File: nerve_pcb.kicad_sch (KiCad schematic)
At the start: 46 parts, among them J1 TC2050-IDC, J2 2171750001, J4 472192001, J5 2x8, J6 2x15, SW1 SPST, SW2 SPST, U1 ld39150dt33-r, U2 STM32F446RET, Y1 8M, Y2 32k768

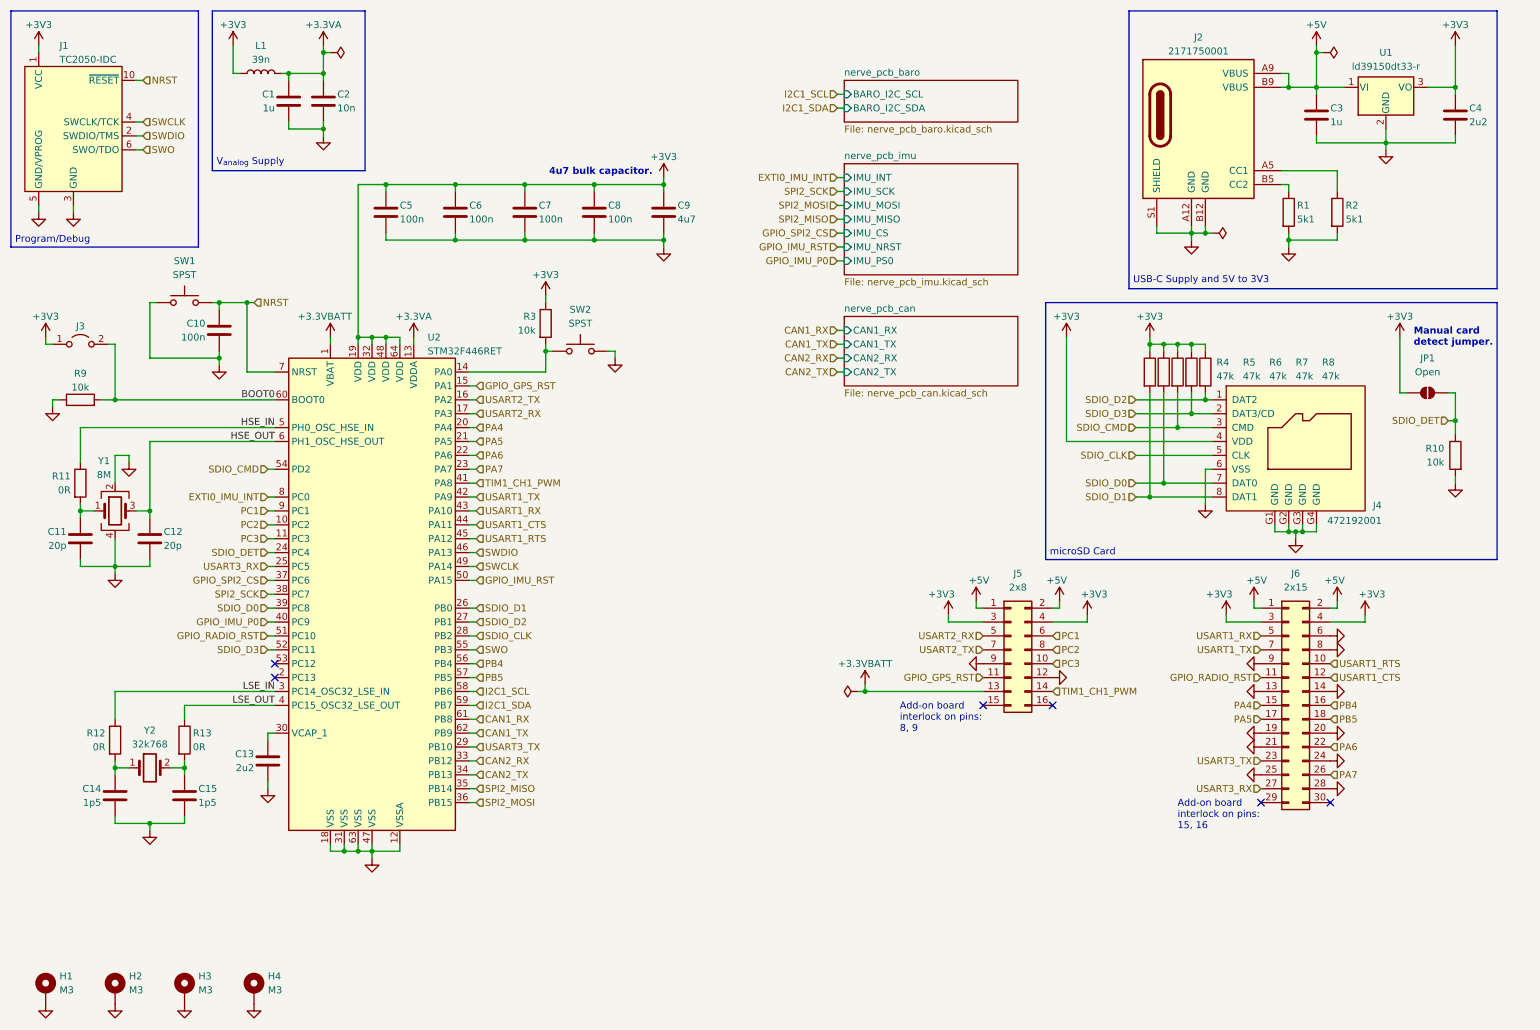
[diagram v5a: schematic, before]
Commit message: Clean up schematics and ensure PCB parity
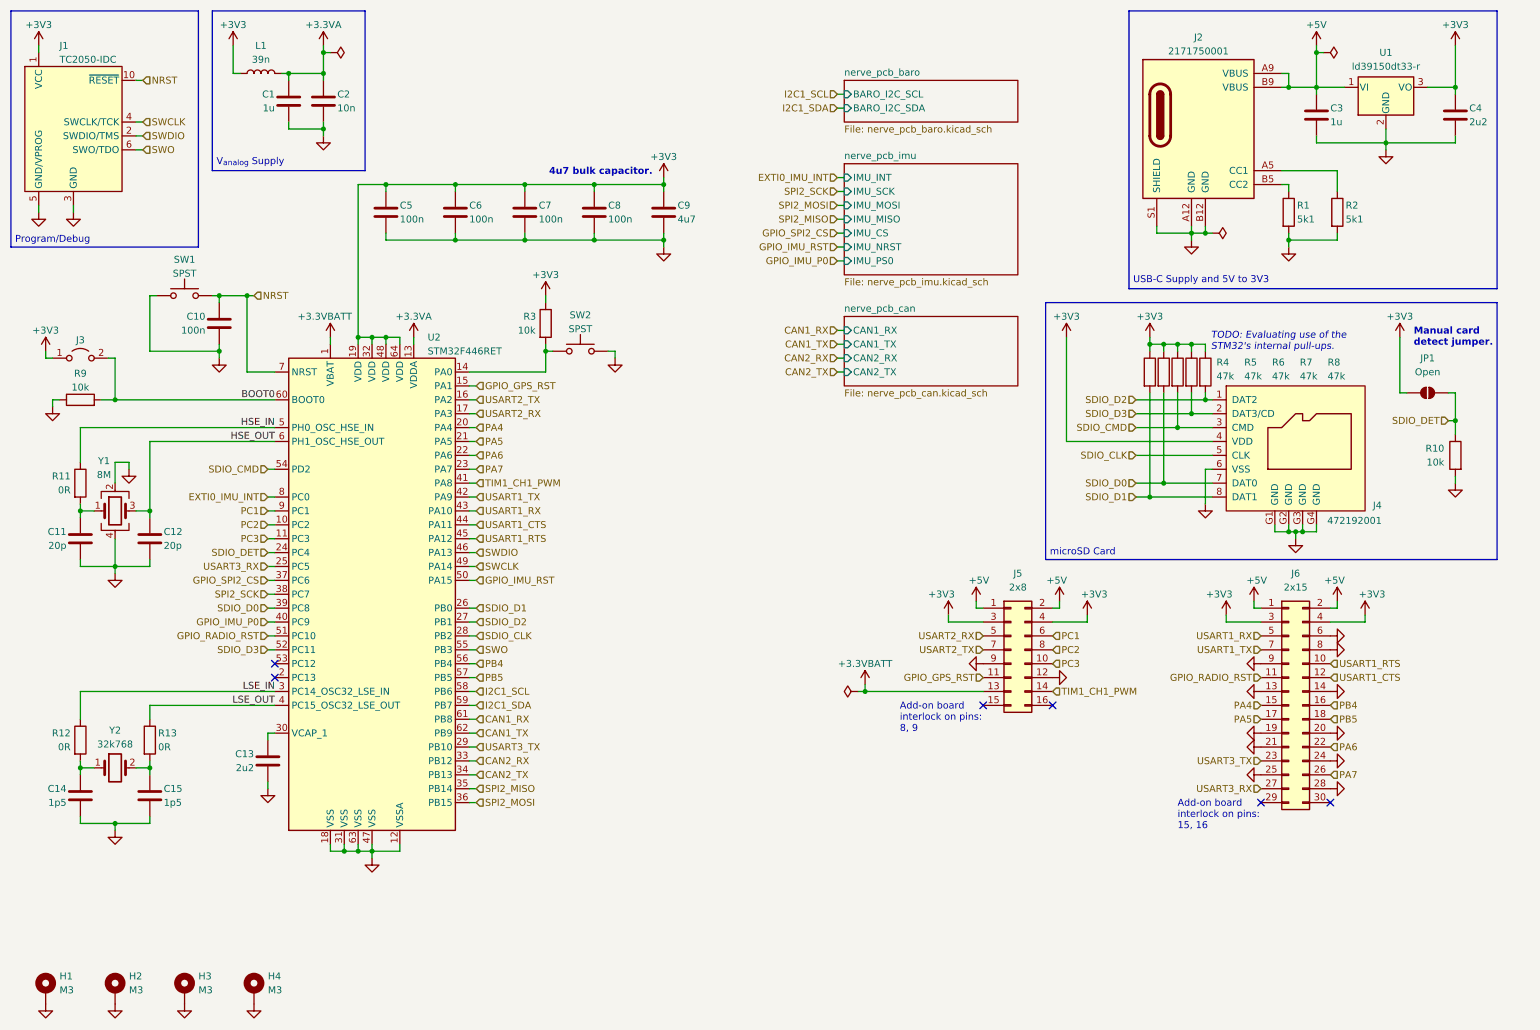
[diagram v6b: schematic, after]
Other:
- note added: "TODO: Evaluating use of the STM32's internal pull-ups."
- moved on the sheet: C10, C14, C15, J3, R12, R13, SW1, Y2

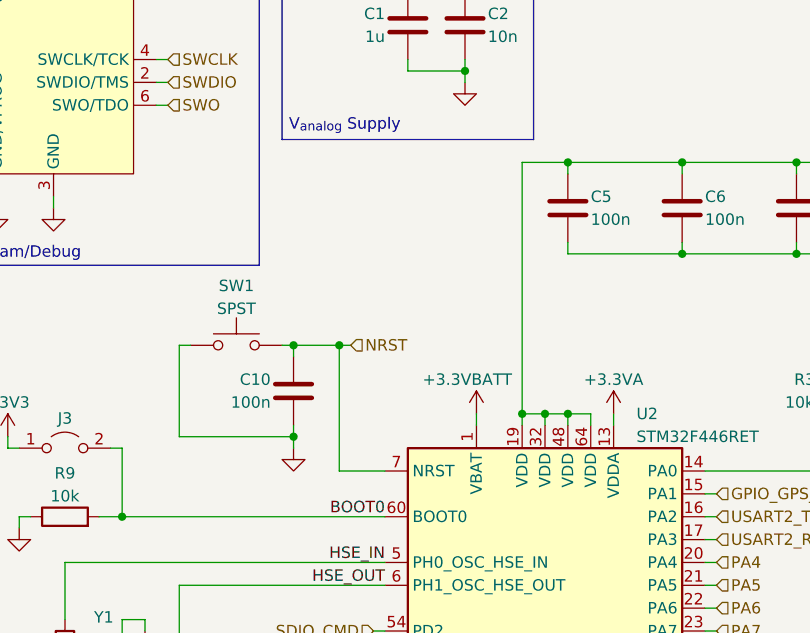
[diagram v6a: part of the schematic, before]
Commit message: Add Vbatt unused jumper
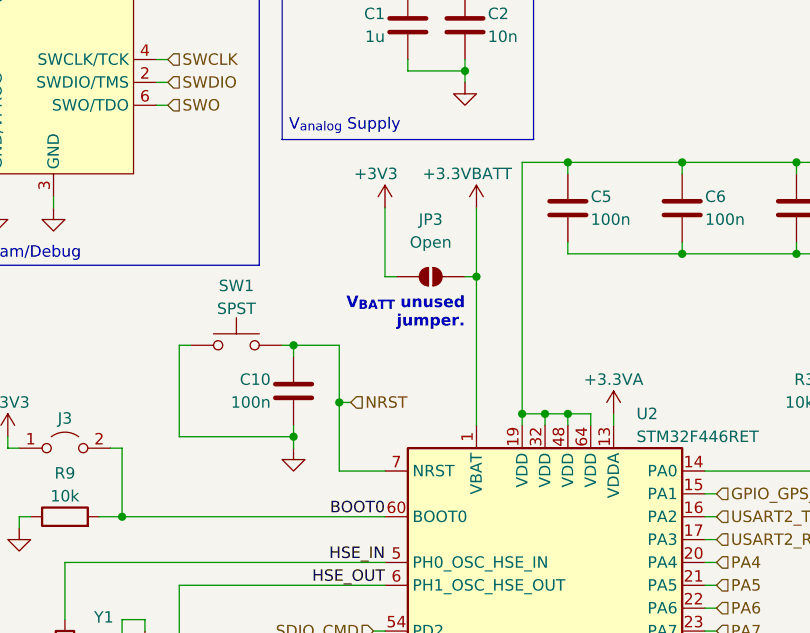
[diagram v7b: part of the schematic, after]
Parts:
- added JP3: Open, Jumper:SolderJumper-2_P1.3mm_Open_TrianglePad1.0x1.5mm, symbol Jumper:SolderJumper_2_Open
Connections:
- net +3.3VBATT: now also JP3.2 (B)
- net +3V3: now also JP3.1 (A)
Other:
- note added: "V_{BATT} unused jumper."
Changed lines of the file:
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@@
 	)
 	(junction
+		(at 71.12 57.15)
+		(diameter 0)
+		(color 0 0 0 0)
+	)
+	(junction
 		(at 246.38 54.61)
 		(diameter 0)
@@
 	)
 	(junction
-		(at 55.88 64.77)
-		(diameter 0)
-		(color 0 0 0 0)
-	)
-	(junction
 		(at 119.38 54.61)
 		(diameter 0)
@@
 	)
 	(junction
+		(at 55.88 71.12)
+		(diameter 0)
+		(color 0 0 0 0)
+	)
+	(junction
 		(at 220.98 101.6)
 		(diameter 0)
@@
 	(wire
 		(pts
+			(xy 71.12 57.15) (xy 71.12 73.66)
+		)
+		(stroke
+			(width 0)
+			(type default)
+		)
+	)
+	(wire
+		(pts
 			(xy 276.86 19.05) (xy 276.86 26.67)
 		)
@@
 	(wire
 		(pts
+			(xy 62.23 57.15) (xy 60.96 57.15)
+		)
+		(stroke
+			(width 0)
+			(type default)
+		)
+	)
+	(wire
+		(pts
 			(xy 38.1 64.77) (xy 38.1 74.93)
 		)
@@
 	(wire
 		(pts
-			(xy 55.88 64.77) (xy 55.88 78.74)
+			(xy 55.88 64.77) (xy 55.88 71.12)
 		)
 		(stroke
@@
 	(wire
 		(pts
+			(xy 60.96 57.15) (xy 60.96 49.53)
+		)
+		(stroke
+			(width 0)
+			(type default)
+		)
+	)
+	(wire
+		(pts
 			(xy 96.52 144.78) (xy 97.79 144.78)
 		)
@@
 	(wire
 		(pts
+			(xy 55.88 71.12) (xy 55.88 78.74)
+		)
+		(stroke
+			(width 0)
+			(type default)
+		)
+	)
+	(wire
+		(pts
 			(xy 31.75 109.22) (xy 31.75 114.3)
 		)
@@
 	(wire
 		(pts
-			(xy 71.12 72.39) (xy 71.12 73.66)
-		)
-		(stroke
-			(width 0)
-			(type default)
-		)
-	)
-	(wire
-		(pts
 			(xy 209.55 124.46) (xy 203.2 124.46)
 		)
@@
 	(wire
 		(pts
+			(xy 71.12 49.53) (xy 71.12 57.15)
+		)
+		(stroke
+			(width 0)
+			(type default)
+		)
+	)
+	(wire
+		(pts
 			(xy 163.83 30.48) (xy 165.1 30.48)
 		)
@@
 	(wire
 		(pts
-			(xy 55.88 64.77) (xy 57.15 64.77)
+			(xy 55.88 71.12) (xy 57.15 71.12)
 		)
 		(stroke
@@
 	(wire
 		(pts
+			(xy 69.85 57.15) (xy 71.12 57.15)
+		)
+		(stroke
+			(width 0)
+			(type default)
+		)
+	)
+	(wire
+		(pts
 			(xy 35.56 25.4) (xy 36.83 25.4)
 		)
@@
 		)
 	)
+	(text "V_{BATT} unused\njumper."
+		(exclude_from_sim no)
+		(at 69.85 61.214 0)
+		(effects
+			(font
+				(size 1.27 1.27)
+				(thickness 0.254)
+				(bold yes)
+			)
+			(justify right)
+		)
+	)
 	(text "USB-C Supply and 5V to 3V3"
 		(exclude_from_sim no)
@@
 	(hierarchical_label "NRST"
 		(shape input)
-		(at 57.15 64.77 0)
+		(at 57.15 71.12 0)
 		(fields_autoplaced yes)
 		(effects
@@
 	(symbol
 		(lib_id "power:+3V3")
-		(at 71.12 72.39 0)
+		(at 71.12 49.53 0)
 		(unit 1)
 		(exclude_from_sim no)
@@
 		(dnp no)
 		(property "Reference" "#PWR015"
-			(at 71.12 76.2 0)
+			(at 71.12 53.34 0)
 			(effects
 				(font
@@
 		)
 		(property "Value" "+3.3VBATT"
-			(at 70.104 68.58 0)
+			(at 70.104 45.72 0)
 			(effects
 				(font
@@
 		)
 		(property "Footprint" ""
-			(at 71.12 72.39 0)
+			(at 71.12 49.53 0)
 			(effects
 				(font
@@
 		)
 		(property "Datasheet" ""
-			(at 71.12 72.39 0)
+			(at 71.12 49.53 0)
 			(effects
 				(font
@@
 		)
 		(property "Description" "Power symbol creates a global label with name \"+3V3\""
-			(at 71.12 72.39 0)
+			(at 71.12 49.53 0)
 			(effects
 				(font
@@
 	)
 	(symbol
+		(lib_id "Jumper:SolderJumper_2_Open")
+		(at 66.04 57.15 0)
+		(unit 1)
+		(exclude_from_sim yes)
+		(in_bom no)
+		(on_board yes)
+		(dnp no)
+		(property "Reference" "JP3"
+			(at 66.04 50.8 0)
+			(effects
+				(font
+					(size 1.27 1.27)
+				)
+			)
+		)
+		(property "Value" "Open"
+			(at 66.04 53.34 0)
+			(effects
+				(font
+					(size 1.27 1.27)
+				)
+			)
+		)
+		(property "Footprint" "Jumper:SolderJumper-2_P1.3mm_Open_TrianglePad1.0x1.5mm"
+			(at 66.04 57.15 0)
+			(effects
+				(font
+					(size 1.27 1.27)
+				)
+				(hide yes)
+			)
+		)
+		(property "Datasheet" "~"
+			(at 66.04 57.15 0)
+			(effects
+				(font
+					(size 1.27 1.27)
+				)
+				(hide yes)
+			)
+		)
+		(property "Description" "Solder Jumper, 2-pole, open"
+			(at 66.04 57.15 0)
+			(effects
+				(font
+					(size 1.27 1.27)
+				)
+				(hide yes)
+			)
+		)
+		(pin "1"
+		)
+		(pin "2"
+		)
+		(instances
+			(project "nerve_pcb"
+				(path "/c0277862-b3f2-4e0e-986f-34702f0543f0"
+					(reference "JP3")
+					(unit 1)
+				)
+			)
+		)
+	)
+	(symbol
 		(lib_id "power:GND")
 		(at 78.74 167.64 0)
@@
 					(unit 1)
 				)
+			)
+		)
+	)
+	(symbol
+		(lib_id "power:+3V3")
+		(at 60.96 49.53 0)
+		(unit 1)
+		(exclude_from_sim no)
+		(in_bom yes)
+		(on_board yes)
+		(dnp no)
+		(property "Reference" "#PWR082"
+			(at 60.96 53.34 0)
+			(effects
+				(font
+					(size 1.27 1.27)
+				)
+				(hide yes)
+			)
+		)
+		(property "Value" "+3V3"
+			(at 59.944 45.72 0)
+			(effects
+				(font
+					(size 1.27 1.27)
+				)
+			)
+		)
+		(property "Footprint" ""
+			(at 60.96 49.53 0)
+			(effects
+				(font
+					(size 1.27 1.27)
+				)
+				(hide yes)
+			)
+		)
+		(property "Datasheet" ""
+			(at 60.96 49.53 0)
+			(effects
+				(font
+					(size 1.27 1.27)
+				)
+				(hide yes)
+			)
+		)
+		(property "Description" "Power symbol creates a global label with name \"+3V3\""
+			(at 60.96 49.53 0)
+			(effects
+				(font
+					(size 1.27 1.27)
+				)
+				(hide yes)
+			)
+		)
+		(pin "1"
+		)
+		(instances
+			(project "nerve_pcb"
+				(path "/c0277862-b3f2-4e0e-986f-34702f0543f0"
+					(reference "#PWR082")
+					(unit 1)
+				)

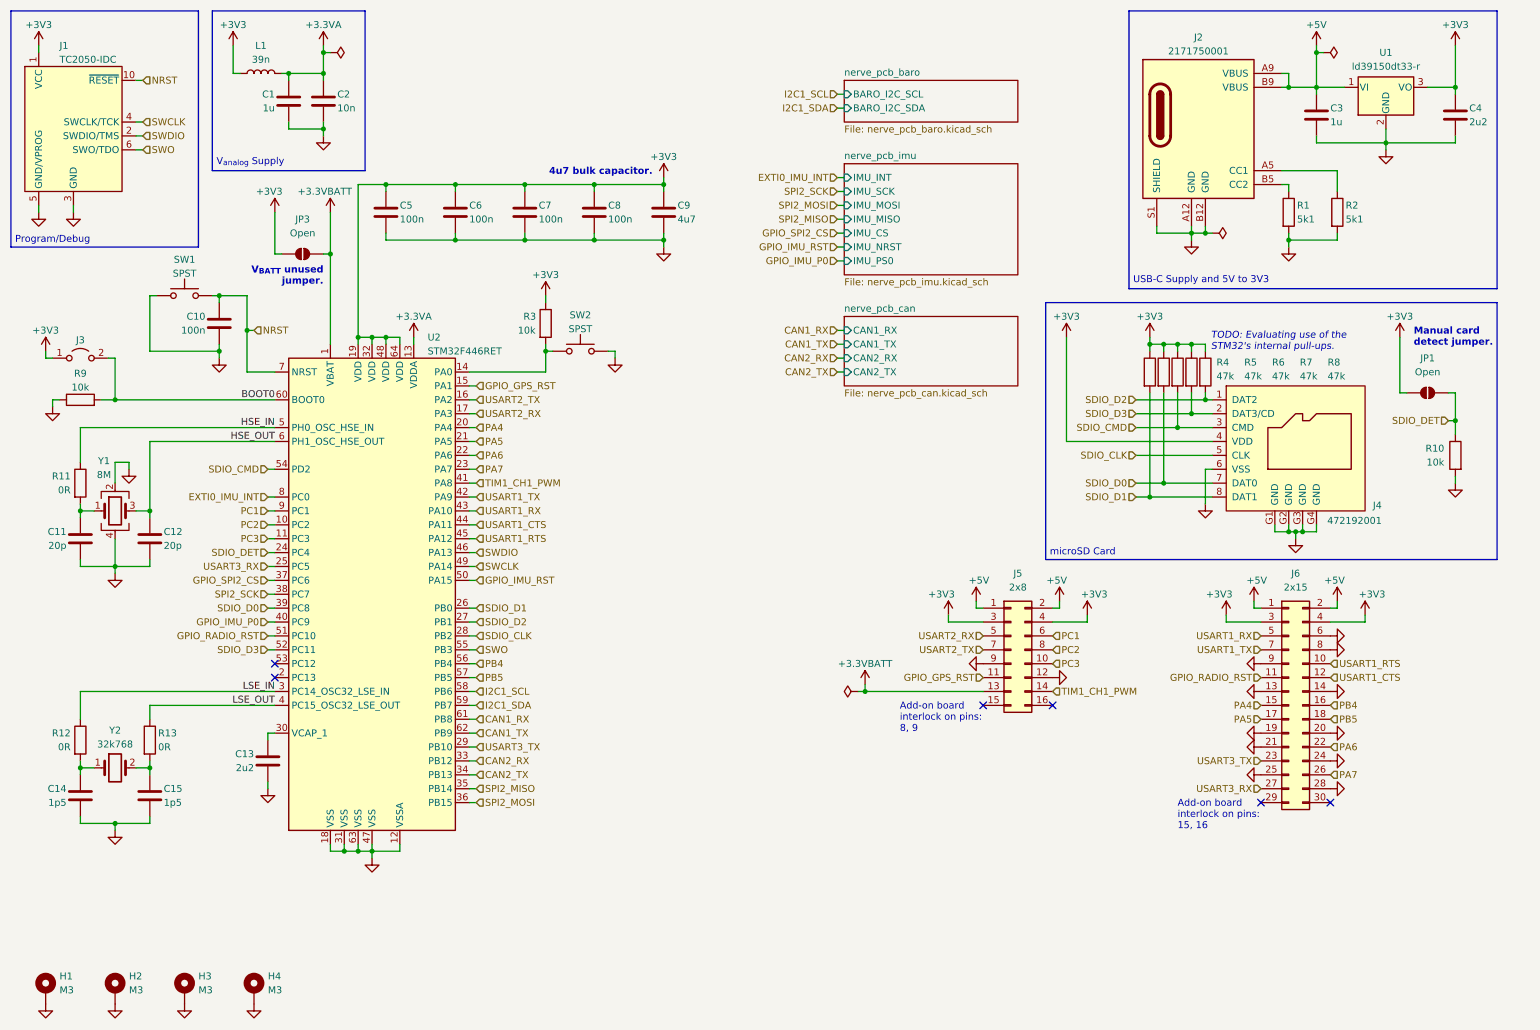
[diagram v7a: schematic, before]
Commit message: Cleanup Vbatt circuit and fix silkscreen
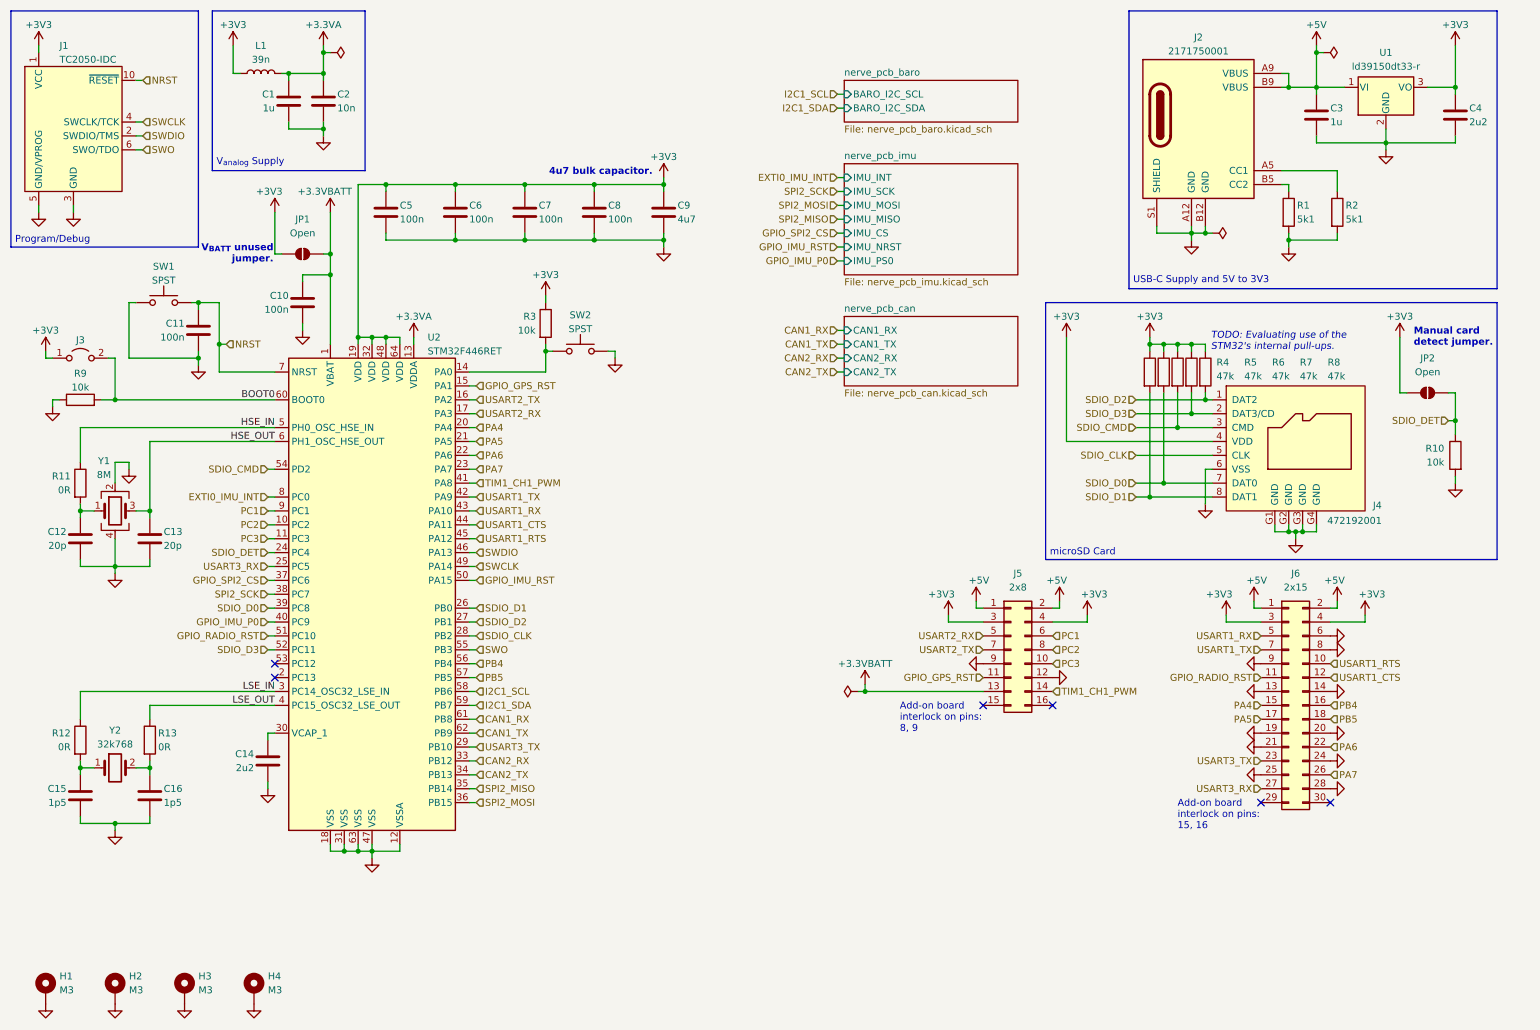
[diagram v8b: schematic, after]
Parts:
- added C10: 100n, Capacitor_SMD:C_0603_1608Metric, symbol Device:C
- renumbered C10 to C11, C11 to C12, C12 to C13, C13 to C14, C14 to C15, C15 to C16, JP3 to JP1, JP1 to JP2
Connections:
- net +3.3VBATT: now also C10.1
- net GND: now also C10.2
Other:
- moved on the sheet: C11, SW1
